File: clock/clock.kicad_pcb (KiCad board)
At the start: 2 copper layers, 100 x 50 mm, 165 parts, among them J1 Conn_02x05_Odd_Even, P1 Conn_WallPlug, U1 74HC596, U10 74HC596, U11 LPC804-TSSOP24, U2 74HC596, U3 74HC596, U4 74HC596, U5 74HC596, U6 74HC596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

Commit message: saving progress
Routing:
- net M40: track 0.00 -> 107.7 mm, vias 0 -> 6
- net M25: track 0.00 -> 96.1 mm, vias 0 -> 6
- net M09: track 0.00 -> 73.4 mm, vias 0 -> 7
- net M10: track 0.00 -> 37.1 mm, vias 0 -> 4
- net H08: track 0.00 -> 32.4 mm, vias 0 -> 5
- net M24: track 105.4 -> 109.6 mm
- net Net-(D27-Pad2): track 0.00 -> 3.42 mm
- net Net-(D41-Pad2): track 0.00 -> 3.25 mm
- net Net-(D48-Pad2): track 0.00 -> 3.17 mm
- net Net-(D51-Pad2): track 0.00 -> 3.05 mm
- net Net-(D45-Pad2): track 0.00 -> 3.04 mm
- net M53: track 65.9 -> 67.6 mm
- net M55: track 66.8 -> 67.4 mm

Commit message: Now we are at the hardest LEDs
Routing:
- net H09: track 0.00 -> 23.3 mm, vias 0 -> 4
- net M10: track 37.1 -> 55.8 mm, vias 4 -> 6
- net M24: track 109.6 -> 116.3 mm
- net Net-(D52-Pad2): track 0.00 -> 4.03 mm
- net M25: track 96.1 -> 99.6 mm
- net Net-(D55-Pad2): track 0.00 -> 3.14 mm
- net Net-(D49-Pad2): track 0.00 -> 3.07 mm
- net Net-(D46-Pad2): track 0.00 -> 3.03 mm
- net M40: track 107.7 -> 110.7 mm
- net M52: track 82.7 -> 85.1 mm
- net M23: track 69.2 -> 71.2 mm
- net H08: track 32.4 -> 34.1 mm
- net M54: track 71.6 -> 73.3 mm
- net M55: track 67.4 -> 68.8 mm
- net M39: track 67.8 -> 69.3 mm
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
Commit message: saving progress
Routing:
- net M56: track 0.00 -> 131.5 mm, vias 0 -> 5
- net M41: track 0.00 -> 79.8 mm, vias 0 -> 4
- net M31: track 81.4 -> 100.9 mm
- net Net-(D32-Pad2): track 0.00 -> 3.38 mm
- net H01: track 26.9 -> 29.6 mm
- net H02: track 20.9 -> 22.9 mm
- net M00: track 55.2 -> 56.6 mm
- net M01: track 37.0 -> 38.1 mm
- net M05: track 68.0 -> 68.7 mm
- net M16: track 71.9 -> 72.6 mm
- net M48: track 69.1 -> 69.7 mm
- net M49: track 69.3 -> 70.0 mm
- net M19: track 49.2 -> 49.8 mm
- net M34: track 73.4 -> 74.0 mm

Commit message: progress saving
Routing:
- net M57: track 0.00 -> 125.5 mm, vias 0 -> 5
- net M26: track 0.00 -> 87.6 mm, vias 0 -> 2
- net M11: track 0.00 -> 47.5 mm, vias 0 -> 4
- net H10: track 0.00 -> 33.1 mm, vias 0 -> 3
- net M58: track 0.00 -> 23.7 mm, vias 0 -> 3
- net H02: track 22.9 -> 26.8 mm, vias 3 -> 4
- net Net-(D54-Pad2): track 0.00 -> 3.49 mm
- net Net-(D50-Pad2): track 0.00 -> 3.40 mm
- net M17: track 54.7 -> 57.9 mm
- net M25: track 99.6 -> 96.9 mm
- net M05: track 68.7 -> 66.2 mm, vias 4 -> 6
- net H01: track 29.6 -> 27.1 mm
- net M00: track 56.6 -> 58.8 mm
- net M45: track 57.1 -> 58.6 mm
- net M56: track 131.5 -> 130.1 mm
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
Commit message: 10 LEDs left
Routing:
- net M42: track 0.00 -> 122.3 mm, vias 0 -> 10
- net M27: track 0.00 -> 85.0 mm, vias 0 -> 4
- net M12: track 0.00 -> 45.5 mm, vias 0 -> 3
- net Net-(D59-Pad2): track 0.00 -> 3.24 mm
- net Net-(D53-Pad2): track 0.00 -> 3.20 mm
- net Net-(D56-Pad2): track 0.00 -> 3.02 mm
- net M30: track 86.5 -> 88.4 mm
- net M19: track 49.8 -> 51.6 mm
- net M52: track 85.0 -> 83.6 mm
- net M53: track 67.5 -> 68.7 mm
- net M46: track 50.2 -> 50.9 mm
- net M26: track 87.6 -> 88.2 mm

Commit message: 2 more collums of LEDs
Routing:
- net M58: track 23.7 -> 136.5 mm, vias 3 -> 5
- net M31: track 101.7 -> 86.9 mm
- net M43: track 0.00 -> 3.81 mm, vias 0 -> 1
- net Net-(D42-Pad2): track 0.00 -> 3.27 mm
- net Net-(D37-Pad2): track 0.00 -> 3.12 mm
- net Net-(D60-Pad2): track 0.00 -> 3.04 mm
- net Net-(D63-Pad2): track 0.00 -> 3.04 mm
- net Net-(D57-Pad2): track 0.00 -> 3.03 mm
- net M46: track 50.9 -> 52.5 mm
- net H02: track 26.8 -> 28.2 mm
- net M16: track 73.6 -> 72.6 mm
- net M45: track 58.6 -> 58.0 mm
- net M01: track 39.3 -> 38.7 mm
- net M56: track 130.1 -> 129.6 mm
- net M00: track 58.8 -> 59.3 mm

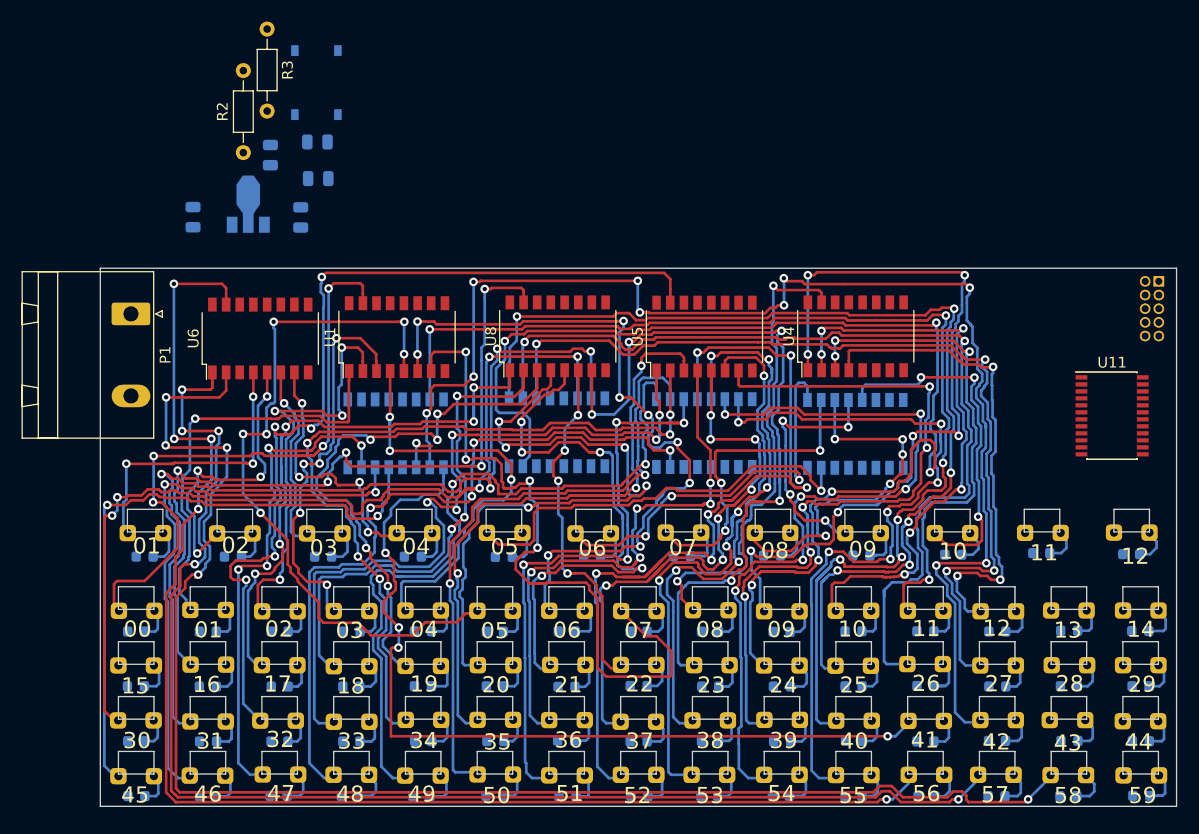
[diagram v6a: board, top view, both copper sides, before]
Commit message: Ran into a trace width issue. Default kicad trace width is 0.25mm or about 9mils. PCBWay can handle 6 mil space or 0.15mm. So I am reducing the traces down to 6 mils. All of them. I am commiting the start of that project
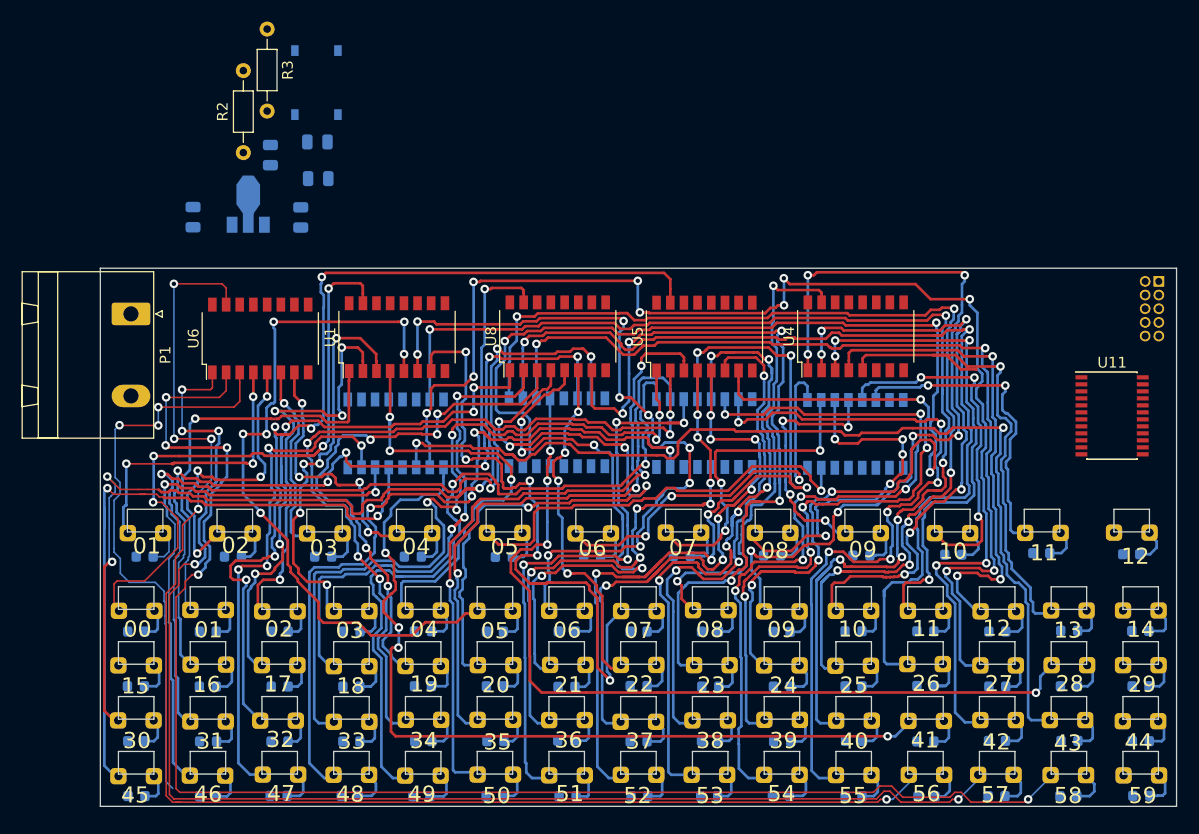
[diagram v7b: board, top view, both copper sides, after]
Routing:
- net M43: track 3.81 -> 92.6 mm, vias 1 -> 2
- net M28: track 0.00 -> 80.0 mm, vias 0 -> 4
- net M59: track 0.00 -> 53.8 mm, vias 0 -> 3
- net M13: track 0.00 -> 46.3 mm, vias 0 -> 1
- net H11: track 0.00 -> 29.0 mm, vias 0 -> 2
- net M07: track 67.2 -> 61.7 mm, vias 4 -> 5
- net M30: track 88.0 -> 91.9 mm
- net M45: track 58.0 -> 61.8 mm
- net M20: track 63.5 -> 66.8 mm
- net M48: track 69.7 -> 72.4 mm
- net M26: track 88.2 -> 90.8 mm
- net M10: track 54.7 -> 57.1 mm
- net M33: track 71.6 -> 73.5 mm
- net M06: track 68.0 -> 69.6 mm
- net M17: track 57.9 -> 56.4 mm
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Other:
- net class PCBWay added: clearance 0.15, trace_width 0.15, via_dia 0.8, via_drill 0.4
- rule trace_min: 0.2 -> 0.15

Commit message: Found the automatic setting to update all trace widths.
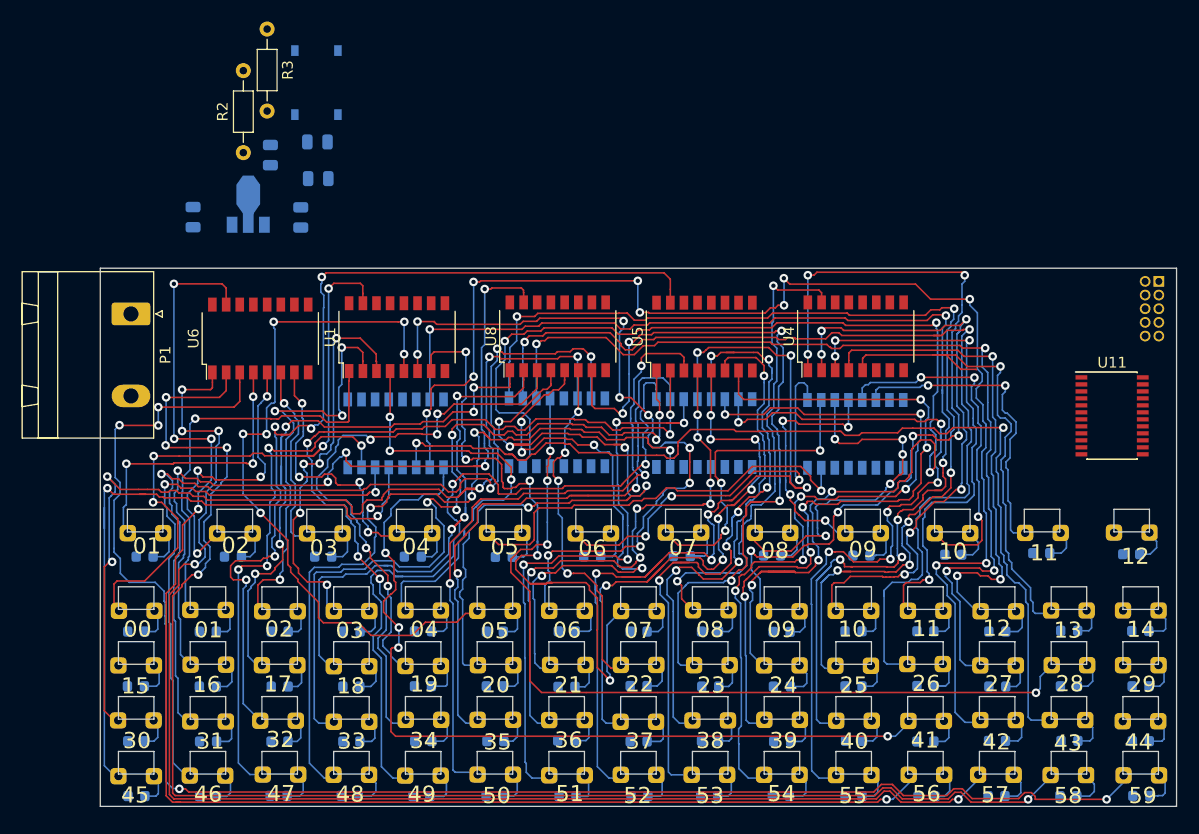
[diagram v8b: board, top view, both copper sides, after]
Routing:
- net M59: track 53.8 -> 145.4 mm, vias 3 -> 5
- net M58: track 135.8 -> 136.7 mm
